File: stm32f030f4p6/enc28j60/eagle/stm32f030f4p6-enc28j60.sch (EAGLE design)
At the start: 33 parts, among them IC2 LM1117IDTX-3.3, IC3 LP2950, X1 MINI-USB-UX60-MB-5ST

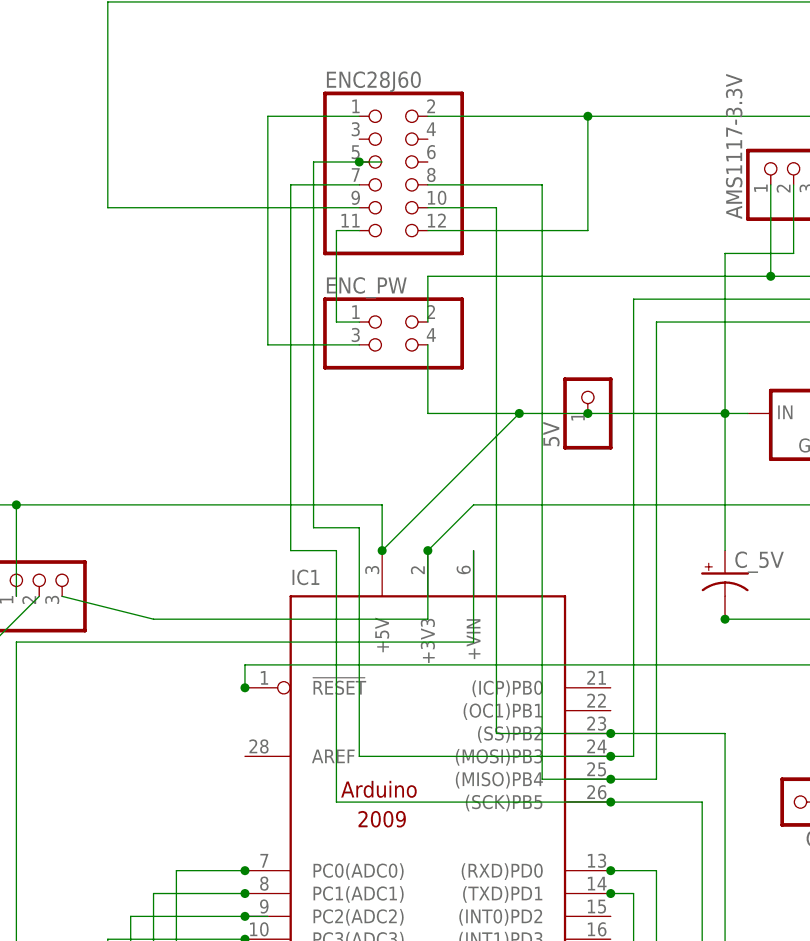
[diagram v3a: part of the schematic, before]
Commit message: Fixed MISO-MOSI
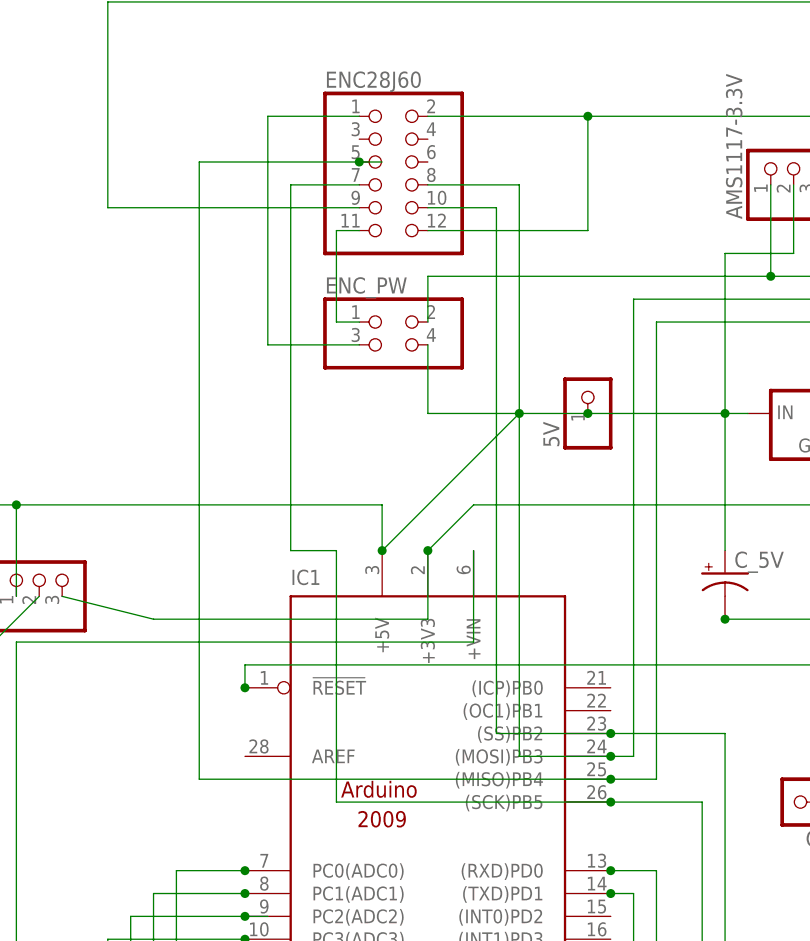
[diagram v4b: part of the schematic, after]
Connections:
- net PA5 renamed PA5_SCK
- removed net PA6: ENC28J60.8, IC1.(MISO)PB4, STM32F030F4PX_R.17, STM32F030F4PX_R.18
- removed net PA7: ENC28J60.5, IC1.(MOSI)PB3, STM32F030F4PX_R.15, STM32F030F4PX_R.16
- new net PA6_MISO: ENC28J60.5, IC1.(MISO)PB4, STM32F030F4PX_R.17, STM32F030F4PX_R.18
- new net PA7_MOSI: ENC28J60.8, IC1.(MOSI)PB3, STM32F030F4PX_R.15, STM32F030F4PX_R.16
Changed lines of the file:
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@@
 </segment>
 </net>
-<net name="PA5" class="0">
+<net name="PA5_SCK" class="0">
 <segment>
 <pinref part="STM32F030F4PX_R" gate="A" pin="19"/>
@@
 </segment>
 </net>
-<net name="PA6" class="0">
+<net name="PA6_MISO" class="0">
 <segment>
 <pinref part="STM32F030F4PX_R" gate="A" pin="18"/>
@@
 <junction x="63.5" y="55.88"/>
 <junction x="137.16" y="33.02"/>
-<pinref part="ENC28J60" gate="A" pin="8"/>
-<wire x1="43.18" y1="121.92" x2="55.88" y2="121.92" width="0.1524" layer="91"/>
-<wire x1="55.88" y1="121.92" x2="55.88" y2="55.88" width="0.1524" layer="91"/>
-<wire x1="55.88" y1="55.88" x2="63.5" y2="55.88" width="0.1524" layer="91"/>
+<wire x1="63.5" y1="55.88" x2="17.78" y2="55.88" width="0.1524" layer="91"/>
+<wire x1="17.78" y1="55.88" x2="17.78" y2="124.46" width="0.1524" layer="91"/>
+<pinref part="ENC28J60" gate="A" pin="5"/>
+<wire x1="38.1" y1="124.46" x2="35.56" y2="124.46" width="0.1524" layer="91"/>
+<wire x1="17.78" y1="124.46" x2="35.56" y2="124.46" width="0.1524" layer="91"/>
+<junction x="35.56" y="124.46"/>
 </segment>
 </net>
@@
 </segment>
 </net>
-<net name="PA7" class="0">
-<segment>
-<pinref part="ENC28J60" gate="A" pin="5"/>
-<wire x1="38.1" y1="124.46" x2="35.56" y2="124.46" width="0.1524" layer="91"/>
-<wire x1="35.56" y1="124.46" x2="30.48" y2="124.46" width="0.1524" layer="91"/>
-<wire x1="30.48" y1="124.46" x2="30.48" y2="83.82" width="0.1524" layer="91"/>
-<junction x="35.56" y="124.46"/>
-<wire x1="30.48" y1="83.82" x2="35.56" y2="83.82" width="0.1524" layer="91"/>
-<wire x1="35.56" y1="83.82" x2="35.56" y2="58.42" width="0.1524" layer="91"/>
+<net name="PA7_MOSI" class="0">
+<segment>
 <pinref part="STM32F030F4PX_R" gate="A" pin="15"/>
 <pinref part="STM32F030F4PX_R" gate="A" pin="16"/>
@@
 <junction x="63.5" y="58.42"/>
 <junction x="137.16" y="35.56"/>
-<wire x1="35.56" y1="58.42" x2="63.5" y2="58.42" width="0.1524" layer="91"/>
-</segment>
-</net>
+<pinref part="ENC28J60" gate="A" pin="8"/>
+<wire x1="53.34" y1="58.42" x2="63.5" y2="58.42" width="0.1524" layer="91"/>
+<wire x1="43.18" y1="121.92" x2="53.34" y2="121.92" width="0.1524" layer="91"/>
+<wire x1="53.34" y1="121.92" x2="53.34" y2="58.42" width="0.1524" layer="91"/>
+</segment>
+</net>
